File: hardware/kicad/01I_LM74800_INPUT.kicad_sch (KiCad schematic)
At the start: 22 parts, among them J901 M8 3pin VEHICLE (external), Q921 STD17NF25 250V, Q922 BUK7Y4R8-60EX 60V, U921 LM74800QDRRRQ1

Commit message: hardware(kicad): resolve three duplicate 01H resistor references and snap 01I nets to KiCad 50mil grid
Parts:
- renumbered R922 to R932, R923 to R933, R924 to R934
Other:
- moved on the sheet: C922, C924, D922, D923, D924, J901, Q921, Q922, R921, R925, R932, R933

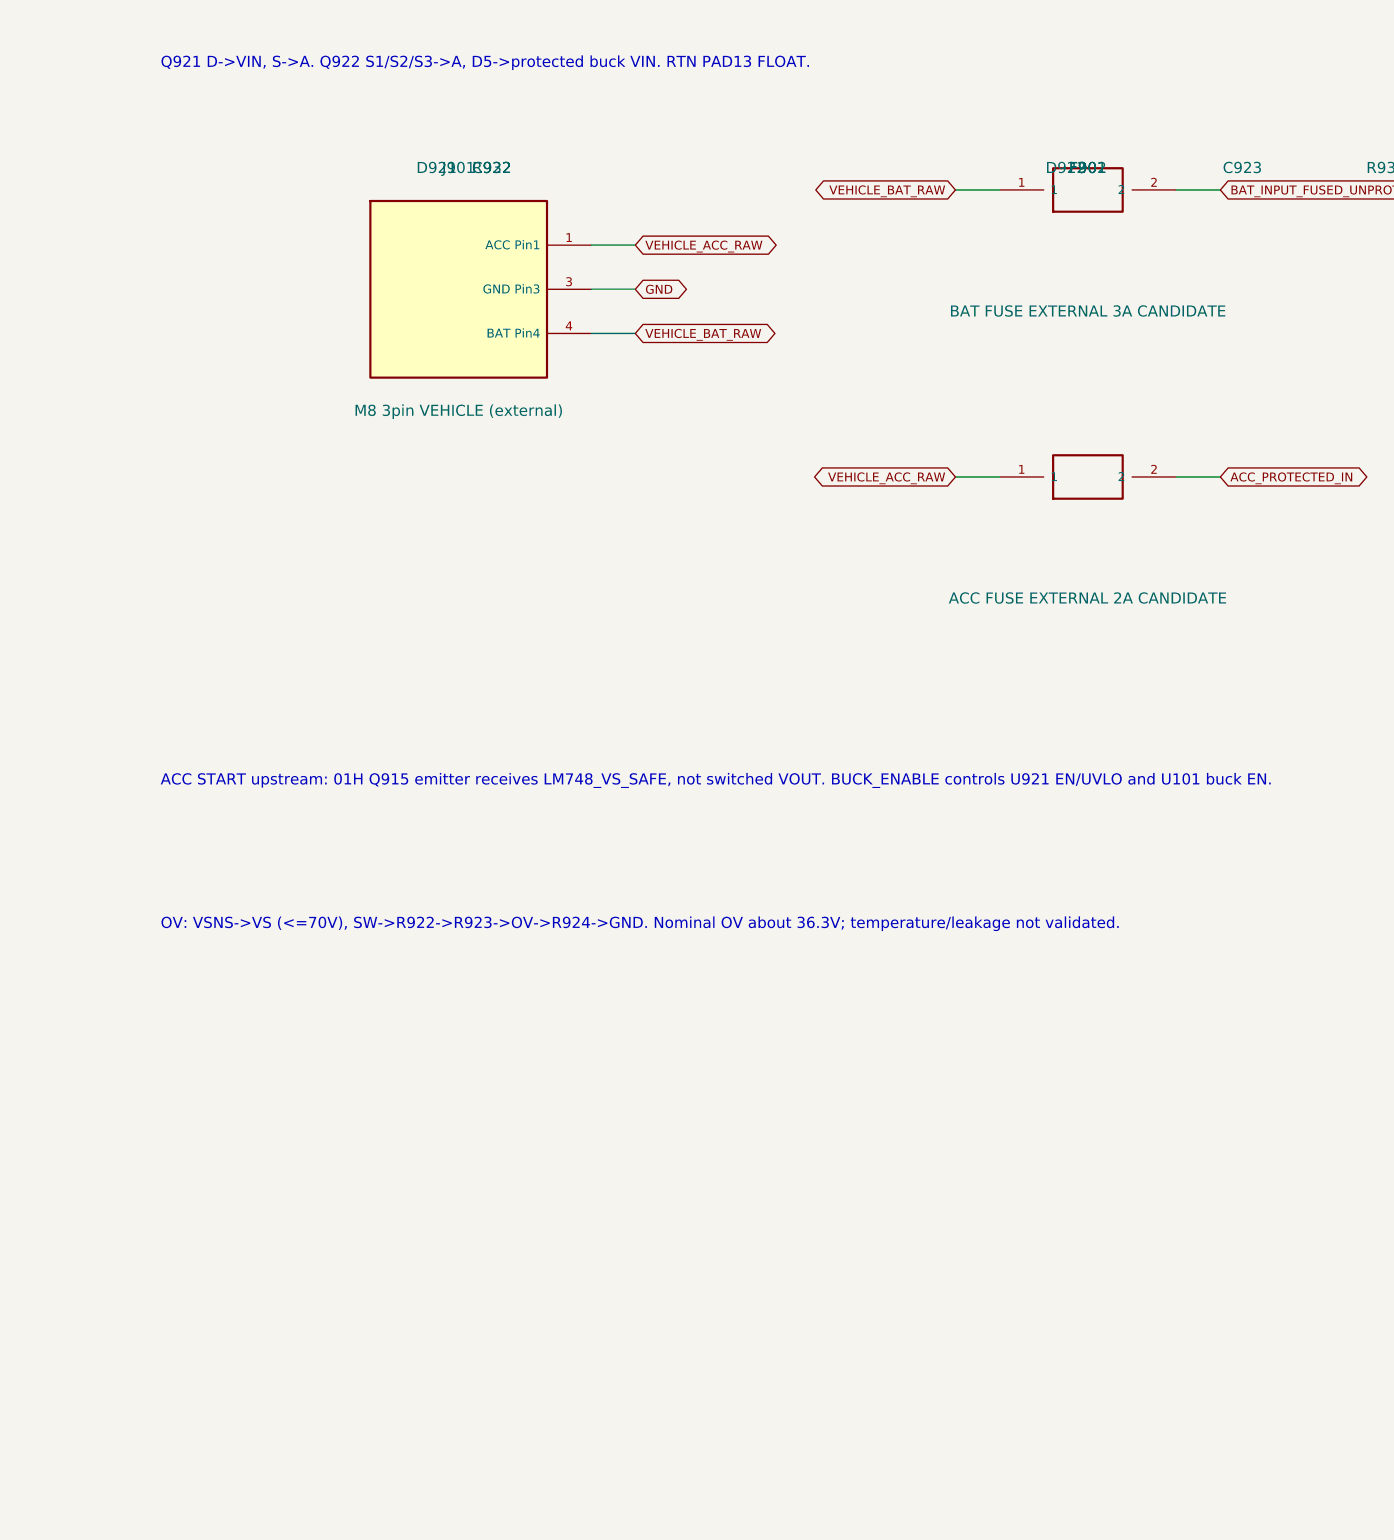
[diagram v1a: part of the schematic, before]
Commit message: hardware: restore J901 on-board three-wire BAT/ACC/GND pigtail and PWR_FLAG; keep M8 and fuses vehicle-external
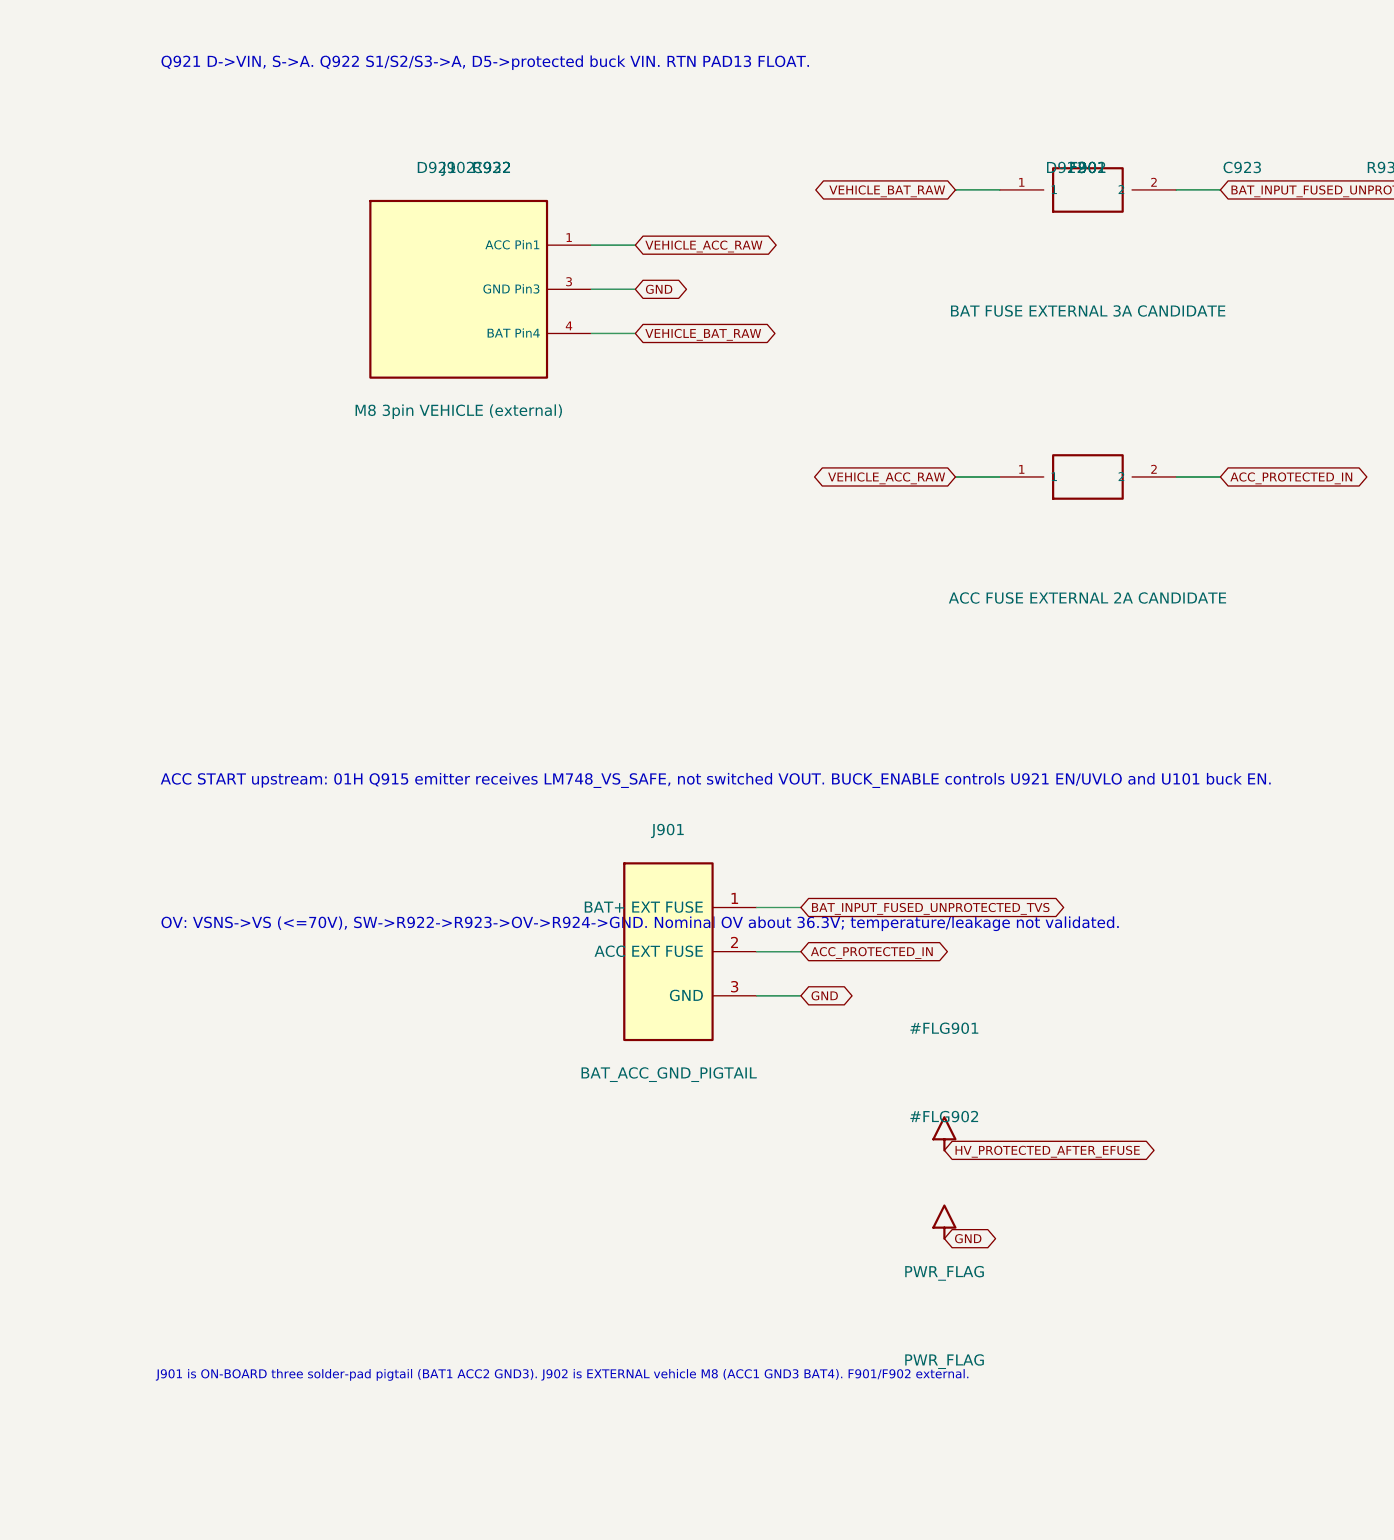
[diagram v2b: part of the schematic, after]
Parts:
- added J901: BAT_ACC_GND_PIGTAIL, Tripmaster:Vehicle_Pigtail_3Wire, symbol TripTracer_V1:POWER_HARNESS_3WIRE
- renumbered J901 to J902
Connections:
- net ACC_PROTECTED_IN: now also J901.2 (ACC EXT FUSE)
- net BAT_INPUT_FUSED_UNPROTECTED_TVS: now also J901.1 (BAT+ EXT FUSE)
- net GND: now also J901.3 (GND)
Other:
- note added: "J901 is ON-BOARD three solder-pad pigtail (BAT1 ACC2 GND3). J902 is EXTERNAL vehicle M8 (ACC1 GND3 BAT4). F901/F902 external."
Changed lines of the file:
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@@
 (title_block (title "TripTracer V1 01I LM74800 input protection") (date "2026-10-14") (rev "WIP - no automotive / ERC release"))
 (symbol (lib_id "TripTracer_V1:VEHICLE_M8_EXTERNAL") (at 64.77 63.5 0) (unit 1) (exclude_from_sim no) (in_bom no) (on_board no) (dnp no)
-(property "Reference" "J901" (at 64.77 49.53 0) (effects (font (size 1.27 1.27))))
+(property "Reference" "J902" (at 64.77 49.53 0) (effects (font (size 1.27 1.27))))
 (property "Value" "M8 3pin VEHICLE (external)" (at 64.77 77.47 0) (effects (font (size 1.27 1.27))))
 (property "Footprint" "" (at 64.77 63.5 0) (effects (font (size 1.27 1.27)) (hide yes)))
@@
 (pin "3")
 (pin "4")
-(instances (project "TripTracer_V1" (path "/a26d9b0c-7f10-4e5a-a65f-000000000064/a26d9b0c-7f10-4e5a-a65f-000000000065" (reference "J901") (unit 1))))
+(instances (project "TripTracer_V1" (path "/a26d9b0c-7f10-4e5a-a65f-000000000064/a26d9b0c-7f10-4e5a-a65f-000000000065" (reference "J902") (unit 1))))
 )
 (symbol (lib_id "TripTracer_V1:PWR_OFFBOARD_FUSE") (at 137.16 52.07 0) (unit 1) (exclude_from_sim no) (in_bom no) (on_board no) (dnp no)
@@
 (text "TI EVM CS C10=15nF on RTN PAD13 to AGND conflicts with datasheet RTN FLOAT; OMIT pending TI clarification. C924=1uF on A to GND." (at 30.48 372.11 0) (effects (font (size 1.27 1.27)) (justify left top)))
 (text "R921 200V/350ms pulse >= 0.7J and VS zener thermal NOT QUALIFIED. NEVER ORDER / USE IN VEHICLE." (at 30.48 406.4 0) (effects (font (size 1.27 1.27)) (justify left top)))
+(symbol (lib_id "TripTracer_V1:POWER_HARNESS_3WIRE") (at 88.9 139.7 0) (unit 1) (exclude_from_sim no) (in_bom yes) (on_board yes) (dnp no)
+(property "Reference" "J901" (at 88.9 125.69999999999999 0) (effects (font (size 1.27 1.27))))
+(property "Value" "BAT_ACC_GND_PIGTAIL" (at 88.9 153.7 0) (effects (font (size 1.27 1.27))))
+(property "Footprint" "Tripmaster:Vehicle_Pigtail_3Wire" (at 88.9 139.7 0) (effects (font (size 1.27 1.27)) (hide yes)))
+(pin "1")
+(pin "2")
+(pin "3")
+(instances (project "TripTracer_V1" (path "/a26d9b0c-7f10-4e5a-a65f-000000000064/a26d9b0c-7f10-4e5a-a65f-000000000065" (reference "J901") (unit 1))))
+)
+(wire (pts (xy 99.06 134.62) (xy 104.14 134.62)) (stroke (width 0) (type default)))
+(global_label "BAT_INPUT_FUSED_UNPROTECTED_TVS" (shape bidirectional) (at 104.14 134.62 0) (effects (font (size 1.016 1.016)) (justify left)))
+(wire (pts (xy 99.06 139.7) (xy 104.14 139.7)) (stroke (width 0) (type default)))
+(global_label "ACC_PROTECTED_IN" (shape bidirectional) (at 104.14 139.7 0) (effects (font (size 1.016 1.016)) (justify left)))
+(wire (pts (xy 99.06 144.78) (xy 104.14 144.78)) (stroke (width 0) (type default)))
+(global_label "GND" (shape bidirectional) (at 104.14 144.78 0) (effects (font (size 1.016 1.016)) (justify left)))
+(symbol (lib_id "TripTracer_V1:EXTERNAL_SUPPLY_FLAG") (at 120.65 162.56 0) (unit 1) (exclude_from_sim no) (in_bom no) (on_board no) (dnp no)
+(property "Reference" "#FLG901" (at 120.65 148.56 0) (effects (font (size 1.27 1.27))))
+(property "Value" "PWR_FLAG" (at 120.65 176.56 0) (effects (font (size 1.27 1.27))))
+(property "Footprint" "" (at 120.65 162.56 0) (effects (font (size 1.27 1.27)) (hide yes)))
+(pin "1")
+(instances (project "TripTracer_V1" (path "/a26d9b0c-7f10-4e5a-a65f-000000000064/a26d9b0c-7f10-4e5a-a65f-000000000065" (reference "#FLG901") (unit 1))))
+)
+(global_label "HV_PROTECTED_AFTER_EFUSE" (shape bidirectional) (at 120.65 162.56 0) (effects (font (size 1.016 1.016)) (justify left)))
+(symbol (lib_id "TripTracer_V1:EXTERNAL_SUPPLY_FLAG") (at 120.65 172.72 0) (unit 1) (exclude_from_sim no) (in_bom no) (on_board no) (dnp no)
+(property "Reference" "#FLG902" (at 120.65 158.72 0) (effects (font (size 1.27 1.27))))
+(property "Value" "PWR_FLAG" (at 120.65 186.72 0) (effects (font (size 1.27 1.27))))
+(property "Footprint" "" (at 120.65 172.72 0) (effects (font (size 1.27 1.27)) (hide yes)))
+(pin "1")
+(instances (project "TripTracer_V1" (path "/a26d9b0c-7f10-4e5a-a65f-000000000064/a26d9b0c-7f10-4e5a-a65f-000000000065" (reference "#FLG902") (unit 1))))
+)
+(global_label "GND" (shape bidirectional) (at 120.65 172.72 0) (effects (font (size 1.016 1.016)) (justify left)))
+(text "J901 is ON-BOARD three solder-pad pigtail (BAT1 ACC2 GND3). J902 is EXTERNAL vehicle M8 (ACC1 GND3 BAT4). F901/F902 external." (at 30 187.96 0) (effects (font (size 1.016 1.016)) (justify left top)))
 (sheet_instances (path "/" (page "2.4")))
 (embedded_fonts no)

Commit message: hardware(kicad): sense OV from raw vehicle BAT per TI 200V cutoff circuit; SW/VSNS clamped, fix symbol reference placement
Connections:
- net BAT_INPUT_FUSED_UNPROTECTED_TVS: now also R932.1
- net LM748_VS_SAFE: now also U921.4 (SW)
- removed net LM748_OV_FEED: R932.1, U921.4 (SW)
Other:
- note added: "OV CUT-OFF TI Fig10-25: VSNS & SW tied to clamped VS (<=70V), R932->R933->OV->R934->GND TOP FED FROM RAW BAT BEFORE Q921. Nominal 36.31V; worst-case limits/open."
- note removed: "OV: VSNS->VS (<=70V), SW->R922->R923->OV->R924->GND. Nominal OV about 36.3V; temperature/leakage not validated."

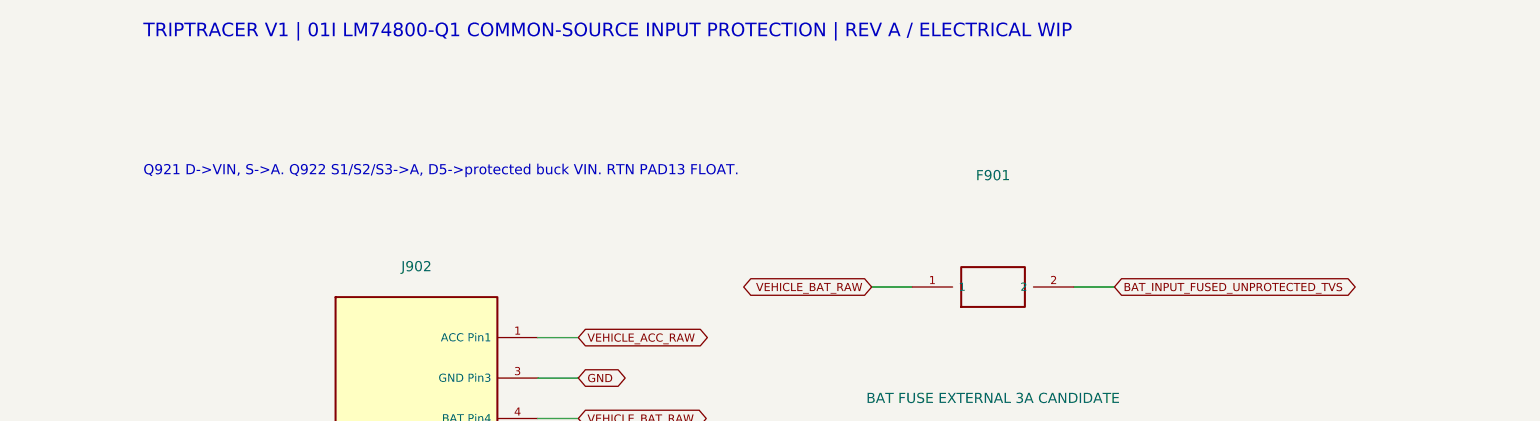
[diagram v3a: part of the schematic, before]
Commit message: hardware(frontend): assign verified TI WSON12 DRR0012E footprint to LM74800 U921; RTN pad remains floating
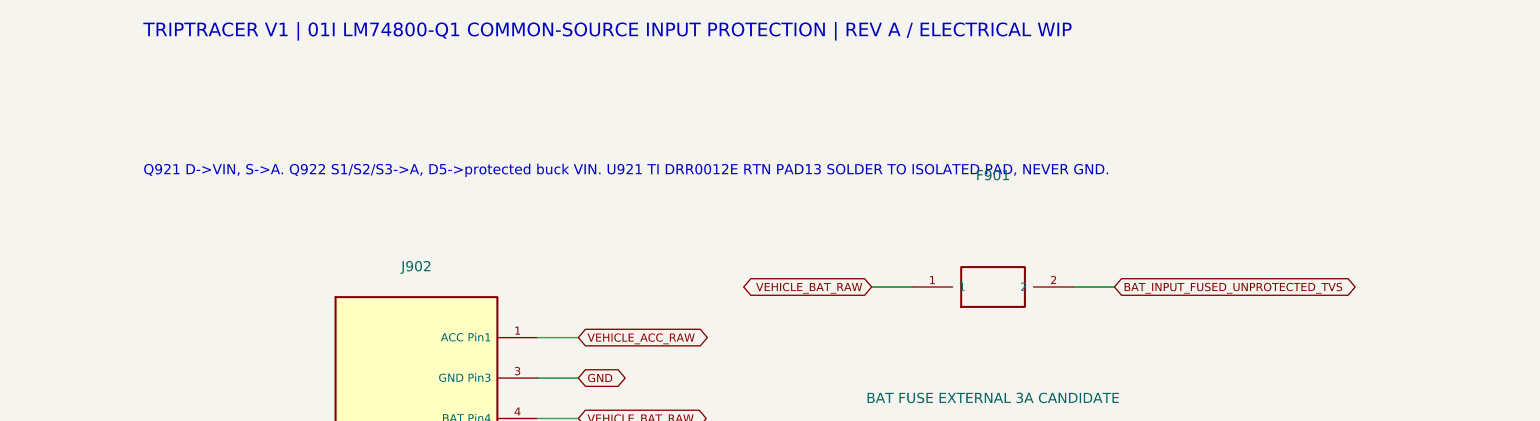
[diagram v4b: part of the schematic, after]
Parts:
- U921: footprint (none) -> Tripmaster:TI_LM74800_Q1_DRR0012E
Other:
- note added: "Q921 D->VIN, S->A. Q922 S1/S2/S3->A, D5->protected buck VIN. U921 TI DRR0012E RTN PAD13 SOLDER TO ISOLATED PAD, NEVER GND."
- note removed: "Q921 D->VIN, S->A. Q922 S1/S2/S3->A, D5->protected buck VIN. RTN PAD13 FLOAT."
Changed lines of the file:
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@@
 (property "Reference" "U921" (at 279.4 154.91 0) (effects (font (size 1.27 1.27))))
 (property "Value" "LM74800QDRRRQ1" (at 279.4 182.88 0) (effects (font (size 1.27 1.27))))
-(property "Footprint" "" (at 279.4 168.91 0) (effects (font (size 1.27 1.27)) (hide yes)))
+(property "Footprint" "Tripmaster:TI_LM74800_Q1_DRR0012E" (at 279.4 168.91 0) (effects (font (size 1.27 1.27)) (hide yes)))
 (property "MPN" "LM74800QDRRRQ1" (at 279.4 168.91 0) (effects (font (size 1.27 1.27)) (hide yes)))
 (pin "1")
@@
 (no_connect (at 304.8 181.61))
 (text "TRIPTRACER V1 | 01I LM74800-Q1 COMMON-SOURCE INPUT PROTECTION | REV A / ELECTRICAL WIP" (at 30.48 19.05 0) (effects (font (size 1.7 1.7)) (justify left top)))
-(text "Q921 D->VIN, S->A. Q922 S1/S2/S3->A, D5->protected buck VIN. RTN PAD13 FLOAT." (at 30.48 36.83 0) (effects (font (size 1.27 1.27)) (justify left top)))
+(text "Q921 D->VIN, S->A. Q922 S1/S2/S3->A, D5->protected buck VIN. U921 TI DRR0012E RTN PAD13 SOLDER TO ISOLATED PAD, NEVER GND." (at 30.48 36.83 0) (effects (font (size 1.27 1.27)) (justify left top)))
 (text "ACC START upstream: 01H Q915 emitter receives LM748_VS_SAFE, not switched VOUT. BUCK_ENABLE controls U921 EN/UVLO and U101 buck EN." (at 30.48 119.38 0) (effects (font (size 1.27 1.27)) (justify left top)))
 (text "OV CUT-OFF TI Fig10-25: VSNS & SW tied to clamped VS (<=70V), R932->R933->OV->R934->GND TOP FED FROM RAW BAT BEFORE Q921. Nominal 36.31V; worst-case limits/open." (at 30.48 135.89 0) (effects (font (size 1.27 1.27)) (justify left top)))
